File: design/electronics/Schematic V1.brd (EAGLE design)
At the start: 152.4 x 139.7 mm, 182 parts, among them J1 PJ-202AH, J3 DD50P564GTXLF, J4 DD50P564GTXLF

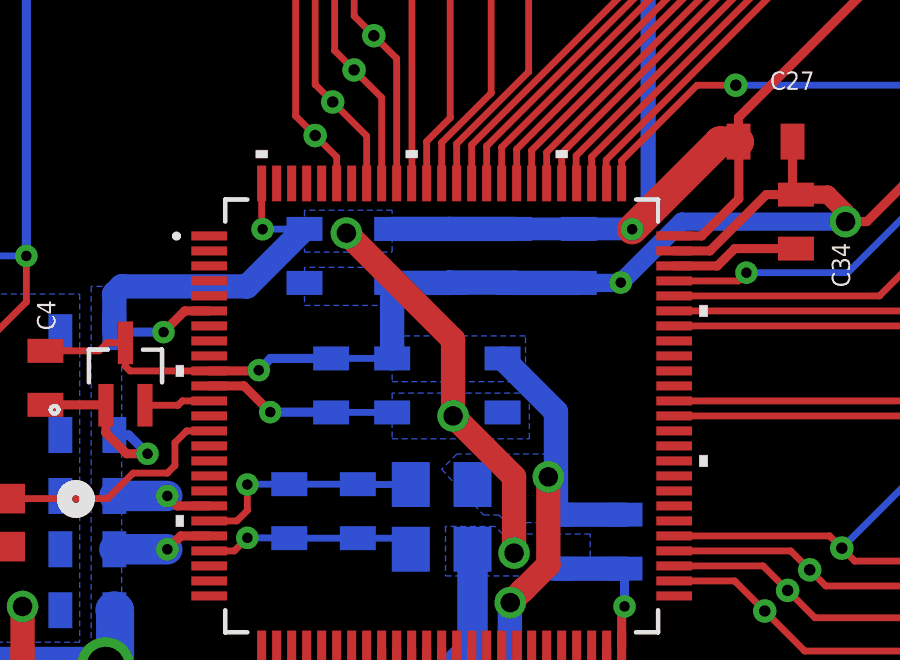
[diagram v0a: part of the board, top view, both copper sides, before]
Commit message: Added Traces
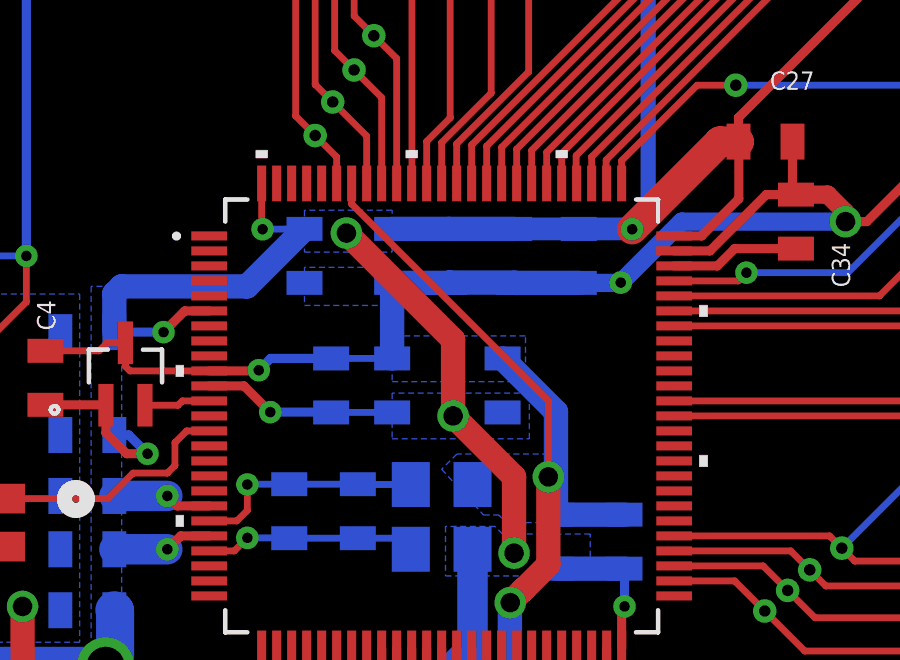
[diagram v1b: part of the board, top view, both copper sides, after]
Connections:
- net S_GND: now also STM32F2.94
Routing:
- net S_GND: track 521.8 -> 534.3 mm
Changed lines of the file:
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@@
 <wire x1="67.9196" y1="95.5548" x2="68.8848" y2="95.5548" width="0.3048" layer="16"/>
 <wire x1="66.305" y1="97.1694" x2="67.9196" y2="95.5548" width="0.3048" layer="16"/>
+<contactref element="STM32F2" pad="94"/>
+<wire x1="81.963" y1="74.806" x2="81.963" y2="74.12" width="0.2286" layer="1"/>
+<wire x1="88.519" y1="67.564" x2="88.519" y2="65.024" width="0.2286" layer="1"/>
+<wire x1="81.963" y1="74.12" x2="88.519" y2="67.564" width="0.2286" layer="1"/>
 </signal>
 <signal name="N$4">

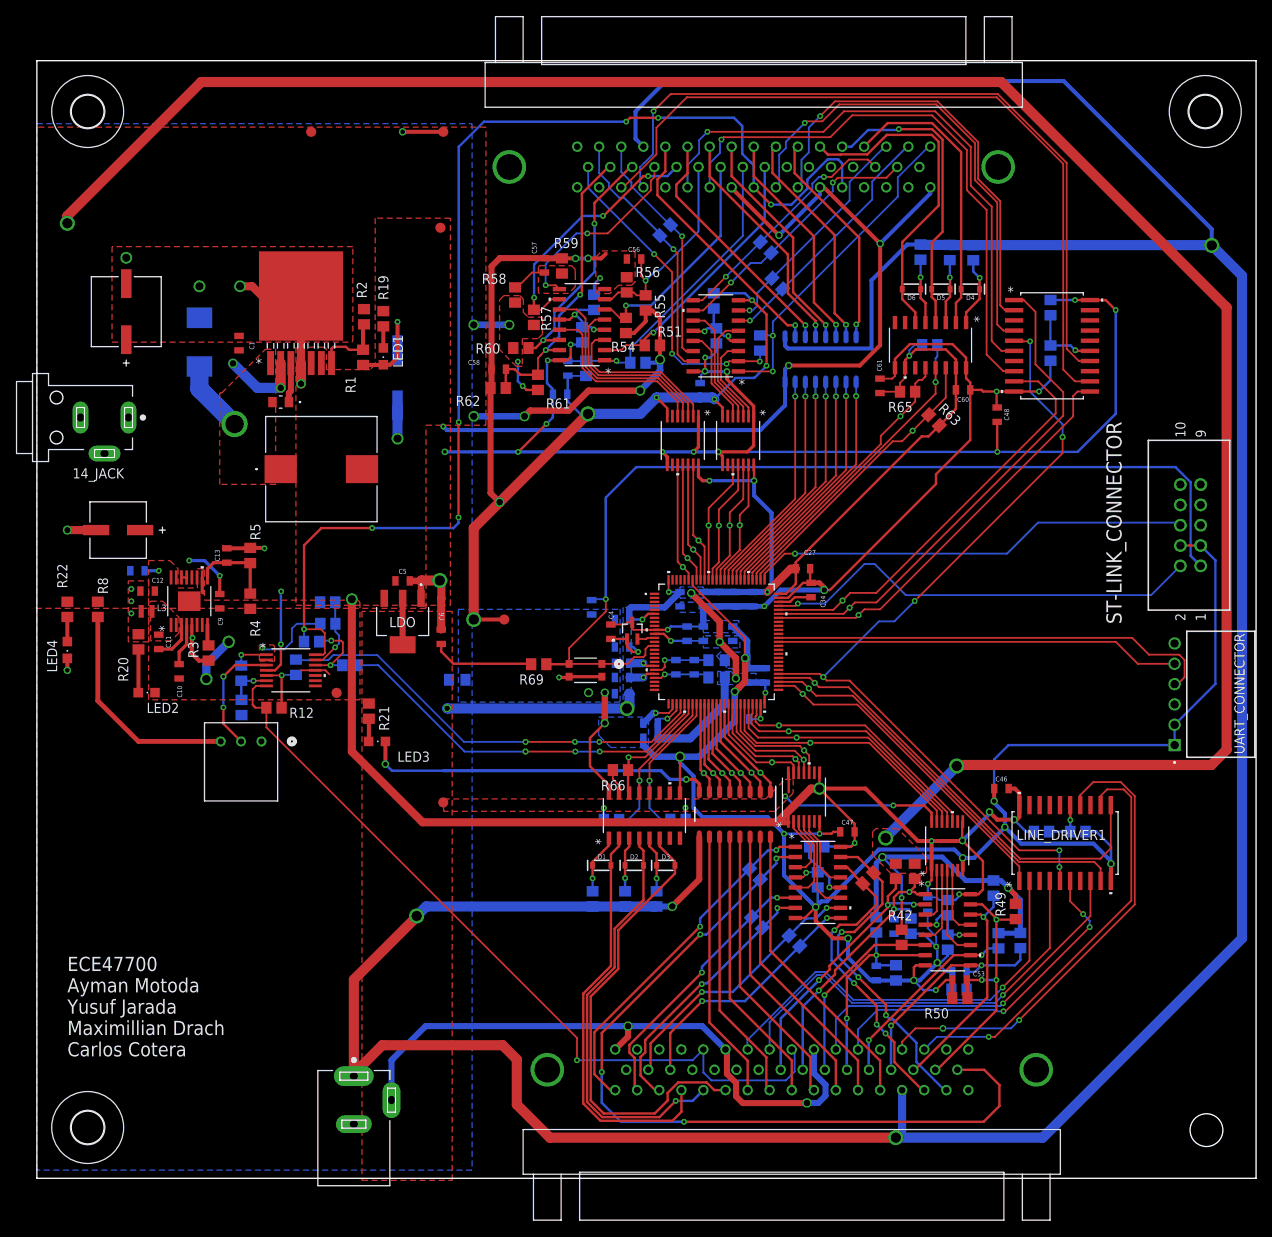
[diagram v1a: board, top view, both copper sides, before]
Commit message: Added jumper connectors to DAC input, added EXT IO Pins
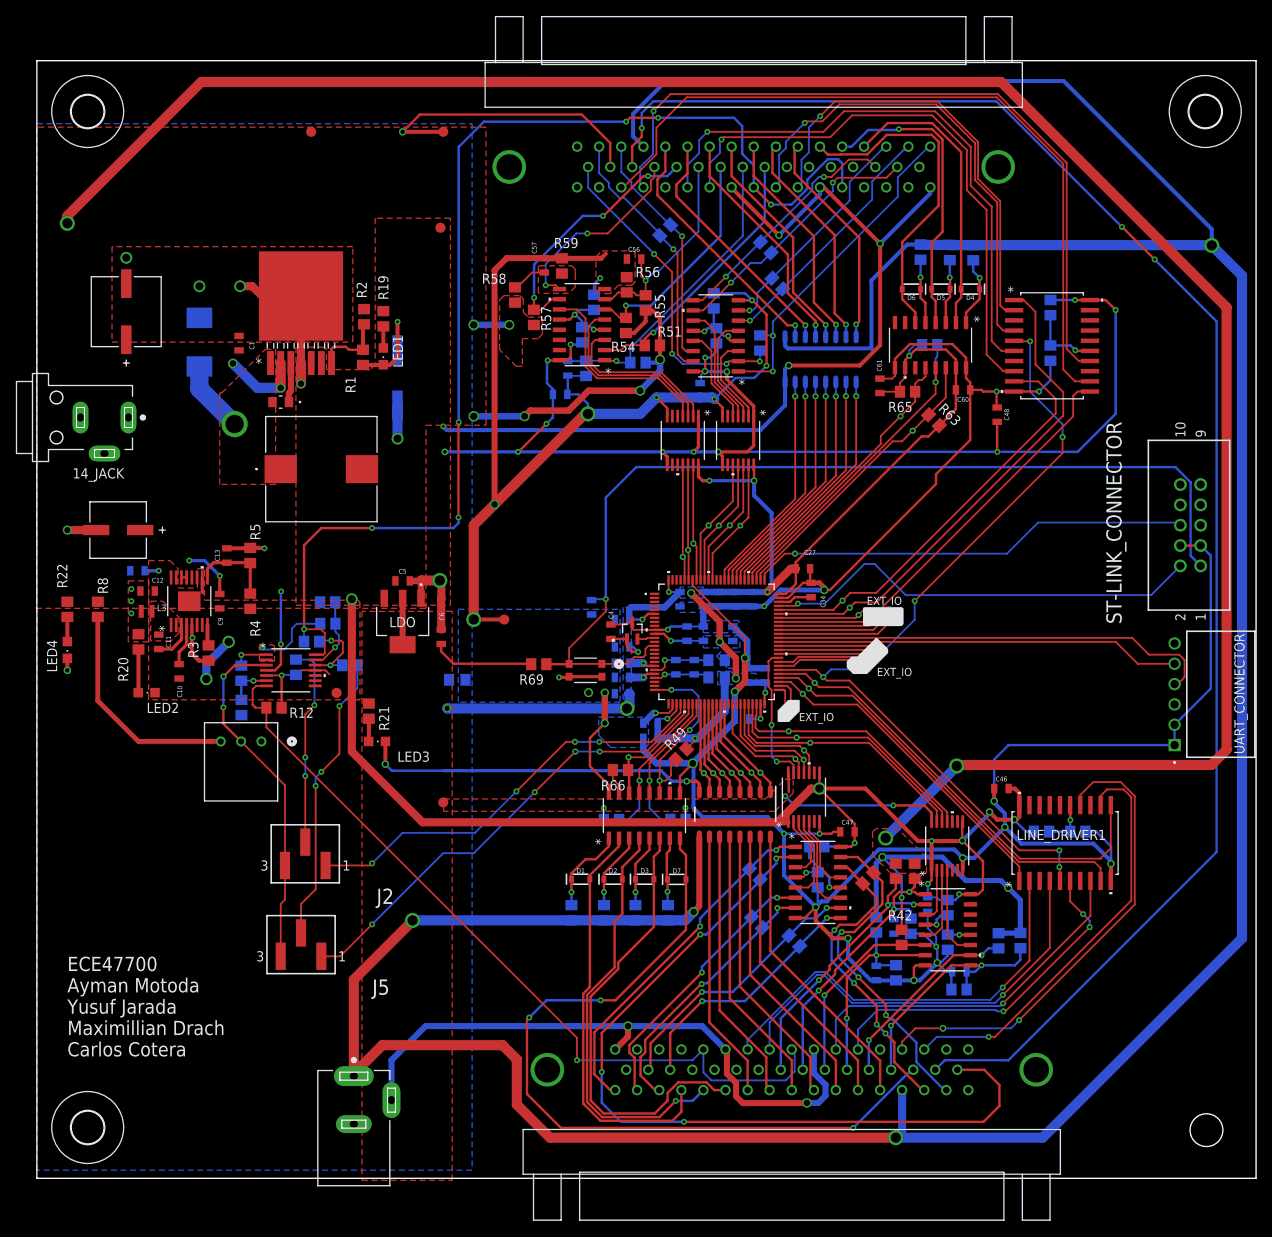
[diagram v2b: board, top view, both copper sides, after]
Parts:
- removed C53, C58: 0.1uF, SparkFun-Capacitors:0805
- removed R50, R62: 25k, rcl:R0805
- removed R60: 500, rcl:R0805
- removed R61: 75k, rcl:R0805
- added D7: 250mA/100V, SparkFun-DiscreteSemi:SOD-323
- added J2, J5: TSM-103-01-L-SVJ, SSW-130-01-G-S:TSM-103-01-L-SV
- R48: value 500 -> 2.25k
- R49: value 75k -> 1k
- moved R49 46.2 mm to (80.5, 53.0), turned to 45 degrees
- moved R48 40.8 mm to (78.9, 33.2), turned to 270 degrees
- moved D1 3.16 mm to (68.0, 37.4)
- moved D2 3.16 mm to (72.0, 37.4)
- moved D3 3.16 mm to (76.0, 37.4)
- moved R17 3.16 mm to (66.8, 33.2)
- moved R18 3.16 mm to (70.9, 33.2)
- moved R27 3.16 mm to (74.8, 33.2)
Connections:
- removed net N$12: OP_AMP.3, R7.2
- removed net SERVO_ALARM_OUT_GPIO_1: LEVEL_SHIFTER1.10, STM32F2.48
- removed net SERVO_ALARM_OUT_GPIO_1_5V: LEVEL_SHIFTER1.5, LINE_RECEIVER2.13
- removed net SERVO_ALARM_OUT_GPIO_2: LEVEL_SHIFTER4.10, STM32F2.95
- removed net SERVO_ALARM_OUT_GPIO_2_5V: LEVEL_SHIFTER4.5, LINE_RECEIVER4.13
- removed net SERVO_ALARM_OUT_HI_1: J3.31, LINE_RECEIVER2.14, R48.1
- removed net SERVO_ALARM_OUT_HI_2: J4.31, LINE_RECEIVER4.14, R60.1
- removed net SERVO_ALARM_OUT_LO_1: C53.2, J3.32, LINE_RECEIVER2.15, R49.1, R50.2
- removed net SERVO_ALARM_OUT_LO_2: C58.2, J4.32, LINE_RECEIVER4.15, R61.1, R62.2
- new net 1.65V: J2.3, J5.3, OP_AMP.3, R7.2
- new net DAC_1_IN: J2.2, R11.1
- new net DAC_2_IN: J5.2, R16.1
- new net EXT_IO1: STM32F2.51
- new net EXT_IO10: STM32F2.67
- new net EXT_IO11: STM32F2.68
- new net EXT_IO2: STM32F2.52
- new net EXT_IO3: STM32F2.57
- new net EXT_IO4: STM32F2.58
- new net EXT_IO5: STM32F2.60
- new net EXT_IO6: STM32F2.61
- new net EXT_IO7: STM32F2.62
- new net EXT_IO8: STM32F2.65
- new net EXT_IO9: STM32F2.66
- new net N$6: D7.C, OPTOCOUPLER.7, R48.1
- new net SERVO_ALARM_AN_1: D7.A, J3.31, OPTOCOUPLER.8
- new net SERVO_ALARM_AN_2: J3.32, J4.31
- new net SERVO_ALARM_GPIO: OPTOCOUPLER.11, R49.1, STM32F2.25
- net +14V: no longer R48.2, R49.2, R60.2, R61.2
- net +24V: now also R48.2
- net +3.3V: now also R49.2
- net ABS_ENC_OUT_GPIO_1: now also STM32F2.45; no longer STM32F2.44
- net ABS_ENC_OUT_GPIO_2: now also STM32F2.92; no longer STM32F2.90
- net CLR_GPIO_1: now also STM32F2.55; no longer STM32F2.54
- net DIR_GPIO_1: now also STM32F2.54; no longer STM32F2.53
- net ENC_PUL_OUT_A_GPIO_1: now also STM32F2.59; no longer STM32F2.41
- net ENC_PUL_OUT_A_GPIO_2: now also STM32F2.89; no longer STM32F2.87
- net ENC_PUL_OUT_B_GPIO_2: now also STM32F2.90; no longer STM32F2.88
- net ENC_PUL_OUT_C_GPIO_1: now also STM32F2.44; no longer STM32F2.43
- net ENC_PUL_OUT_C_GPIO_2: now also STM32F2.91; no longer STM32F2.89
- net GEN_PURPOSE_OUT_GPIO_A_1: now also STM32F2.46; no longer STM32F2.45
- net GEN_PURPOSE_OUT_GPIO_A_2: now also STM32F2.93; no longer STM32F2.91
- net GEN_PURPOSE_OUT_GPIO_B_1: now also STM32F2.47; no longer STM32F2.46
- net GEN_PURPOSE_OUT_GPIO_B_2: now also STM32F2.95; no longer STM32F2.92
- net GEN_PURPOSE_OUT_GPIO_C_1: now also STM32F2.48; no longer STM32F2.47
- net GEN_PURPOSE_OUT_GPIO_C_2: now also STM32F2.96; no longer STM32F2.93
- net POS_EN_GPIO: now also STM32F2.56; no longer STM32F2.55
- net PULSE_GPIO_1: now also STM32F2.53; no longer STM32F2.52
- net P_GND: now also J4.32
- net S_GND: no longer C53.1, C58.1, R50.1, R62.1
- net TORQUE-SPEED_DAC_1: now also J2.1; no longer R11.1
- net TORQUE-SPEED_DAC_2: now also J5.1; no longer R16.1
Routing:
- net SERVO_ALARM_AN_2: track 0.00 -> 203.9 mm, vias 0 -> 3
- net SERVO_ALARM_AN_1: track 0.00 -> 98.6 mm, vias 0 -> 3
- net 1.65V: track 0.00 -> 44.4 mm, vias 0 -> 2
- net SERVO_ALARM_OUT_LO_2: track 38.2 -> 0.00 mm, vias 2 -> 0
- net DAC_2_IN: track 0.00 -> 36.4 mm, vias 0 -> 3
- net SERVO_ALARM_OUT_LO_1: track 34.6 -> 0.00 mm, vias 3 -> 0
- net SERVO_ALARM_OUT_GPIO_1: track 32.7 -> 0.00 mm, vias 1 -> 0
- net P_GND: track 291.9 -> 323.2 mm
- net SERVO_ALARM_OUT_HI_2: track 30.7 -> 0.00 mm, vias 2 -> 0
- net SERVO_ALARM_OUT_HI_1: track 28.2 -> 0.00 mm, vias 1 -> 0
- net DAC_1_IN: track 0.00 -> 25.3 mm, vias 0 -> 3
- net SERVO_ALARM_GPIO: track 0.00 -> 23.9 mm, vias 0 -> 3
- net SERVO_ALARM_OUT_GPIO_2_5V: track 22.7 -> 0.00 mm
- net EXT_IO8: track 0.00 -> 15.6 mm, vias 0 -> 1
- net N$12: track 15.0 -> 0.00 mm, vias 2 -> 0
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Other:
- board text added: "EXT_IO"

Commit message: Finished Design
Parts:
- added LED10: INDIC_LED, led:CHIPLED_0805
- added LED5: UART_LED, led:CHIPLED_0805
- added LED6: POS_CON_LED, led:CHIPLED_0805
- added LED7: ALO1, led:CHIPLED_0805
- added LED8: ALO2, led:CHIPLED_0805
- added LED9: ALO3, led:CHIPLED_0805
- added R50, R60, R61, R62, R77, R78: 150, rcl:R0805
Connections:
- new net ALO1_LED: R61.1, STM32F2.1
- new net ALO2_LED: R62.1, STM32F2.2
- new net ALO3_LED: R77.1, STM32F2.3
- new net INDIC_LED: R78.1, STM32F2.4
- new net N$10: LED6.A, R60.2
- new net N$12: LED7.A, R61.2
- new net N$14: LED8.A, R62.2
- new net N$16: LED9.A, R77.2
- new net N$19: LED10.A, R78.2
- new net N$9: LED5.A, R50.2
- new net POS_CON_LED: R60.1, STM32F2.98
- new net UART_LED: R50.1, STM32F2.97
- net P_GND: now also LED10.C, LED5.C, LED6.C, LED7.C, LED8.C, LED9.C
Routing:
- net P_GND: track 323.2 -> 349.2 mm, vias 22 -> 23
- net UART_LED: track 0.00 -> 16.4 mm
- net POS_CON_LED: track 0.00 -> 14.6 mm
- net ALO1_LED: track 0.00 -> 12.2 mm
- net ALO2_LED: track 0.00 -> 10.2 mm
- net ALO3_LED: track 0.00 -> 9.32 mm
- net INDIC_LED: track 0.00 -> 8.46 mm
- net N$19: track 0.00 -> 2.39 mm
- net N$16: track 0.00 -> 2.39 mm
- net N$14: track 0.00 -> 2.34 mm
- net N$9: track 0.00 -> 2.34 mm
- net N$12: track 0.00 -> 2.33 mm
- net N$10: track 0.00 -> 2.32 mm

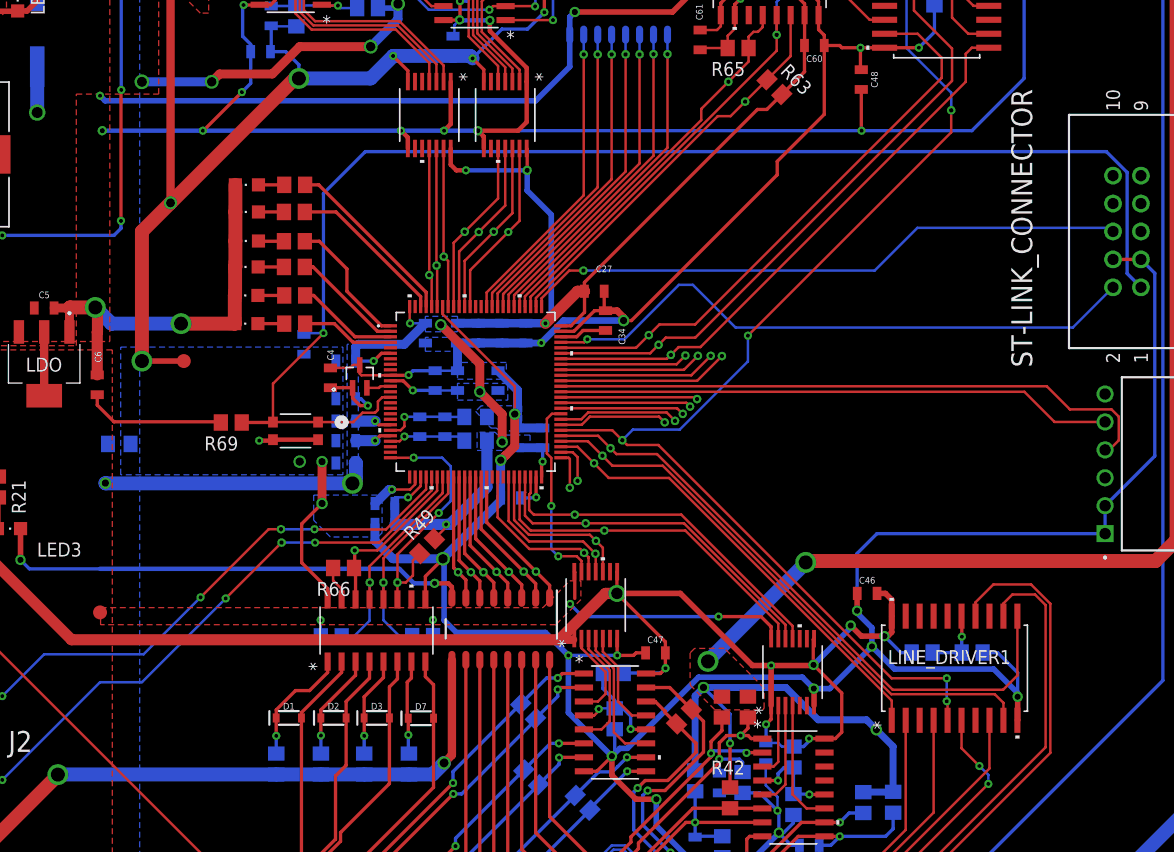
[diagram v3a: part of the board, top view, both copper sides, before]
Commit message: Added pull downs to level shifter 5V lines
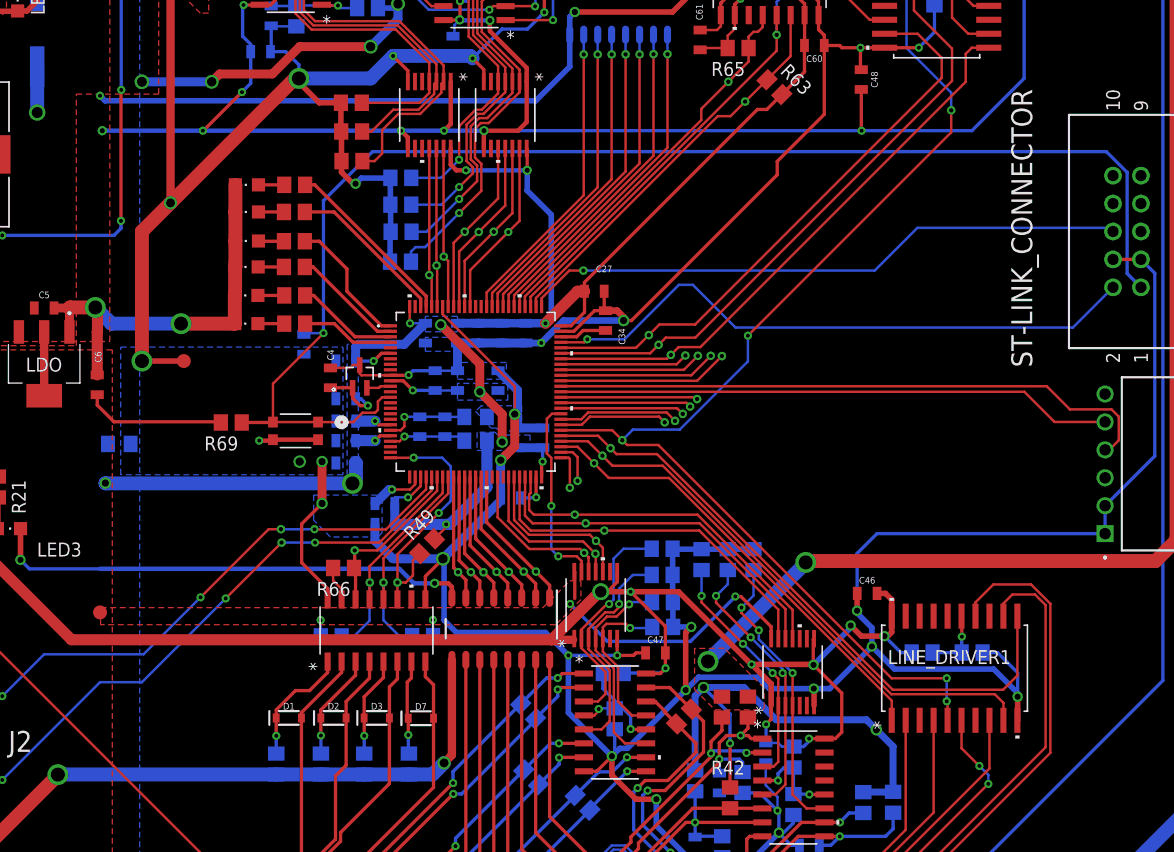
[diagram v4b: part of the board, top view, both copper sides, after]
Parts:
- added R79, R80, R81, R82, R83, R84, R85, R86, R87, R88, R89, R90, R91, R92: 10k, rcl:R0805
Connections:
- net ABS_ENC_OUT_GPIO_1_5V: now also R92.2
- net ABS_ENC_OUT_GPIO_2_5V: now also R88.2
- net ENC_PUL_OUT_A_GPIO_1_5V: now also R91.2
- net ENC_PUL_OUT_A_GPIO_2_5V: now also R87.2
- net ENC_PUL_OUT_B_GPIO_1_5V: now also R90.2
- net ENC_PUL_OUT_B_GPIO_2_5V: now also R86.2
- net ENC_PUL_OUT_C_GPIO_1_5V: now also R89.2
- net ENC_PUL_OUT_C_GPIO_2_5V: now also R85.2
- net GEN_PURPOSE_OUT_GPIO_A_1_5V: now also R81.2
- net GEN_PURPOSE_OUT_GPIO_A_2_5V: now also R84.2
- net GEN_PURPOSE_OUT_GPIO_B_1_5V: now also R80.2
- net GEN_PURPOSE_OUT_GPIO_B_2_5V: now also R83.2
- net GEN_PURPOSE_OUT_GPIO_C_1_5V: now also R79.2
- net GEN_PURPOSE_OUT_GPIO_C_2_5V: now also R82.2
- net S_GND: now also R79.1, R80.1, R81.1, R82.1, R83.1, R84.1, R85.1, R86.1, R87.1, R88.1, R89.1, R90.1, R91.1, R92.1
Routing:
- net S_GND: track 524.6 -> 570.9 mm, vias 32 -> 35
- net ENC_PUL_OUT_A_GPIO_2_5V: track 11.2 -> 33.1 mm, vias 0 -> 1
- net ENC_PUL_OUT_B_GPIO_2_5V: track 14.0 -> 33.2 mm, vias 0 -> 1
- net ENC_PUL_OUT_C_GPIO_2_5V: track 15.1 -> 32.3 mm, vias 0 -> 1
- net GEN_PURPOSE_OUT_GPIO_B_1_5V: track 9.66 -> 25.0 mm, vias 0 -> 3
- net GEN_PURPOSE_OUT_GPIO_A_1_5V: track 6.74 -> 22.0 mm, vias 0 -> 3
- net GEN_PURPOSE_OUT_GPIO_C_1_5V: track 11.5 -> 26.2 mm, vias 0 -> 3
- net ABS_ENC_OUT_GPIO_2_5V: track 12.1 -> 26.0 mm, vias 0 -> 1
- net ENC_PUL_OUT_A_GPIO_1_5V: track 8.19 -> 20.6 mm, vias 0 -> 1
- net GEN_PURPOSE_OUT_GPIO_A_2_5V: track 20.6 -> 32.7 mm
- net ENC_PUL_OUT_B_GPIO_1_5V: track 11.0 -> 20.6 mm, vias 0 -> 1
- net GEN_PURPOSE_OUT_GPIO_B_2_5V: track 23.2 -> 32.4 mm
- net GEN_PURPOSE_OUT_GPIO_C_2_5V: track 25.5 -> 33.0 mm
- net ENC_PUL_OUT_C_GPIO_1_5V: track 12.5 -> 19.6 mm, vias 0 -> 1
- net ABS_ENC_OUT_GPIO_1_5V: track 9.37 -> 15.2 mm, vias 0 -> 1
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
